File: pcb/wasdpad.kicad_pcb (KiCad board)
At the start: 2 copper layers, 64.2 x 61.2 mm, 24 parts, among them SW1 SW_Push_45deg, SW2 SW_Push_45deg, SW3 SW_Push_45deg, SW4 SW_Push_45deg, SW5 SW_Push_45deg, SW6 SW_Push_45deg, U1 XIAO-RP2040-DIP

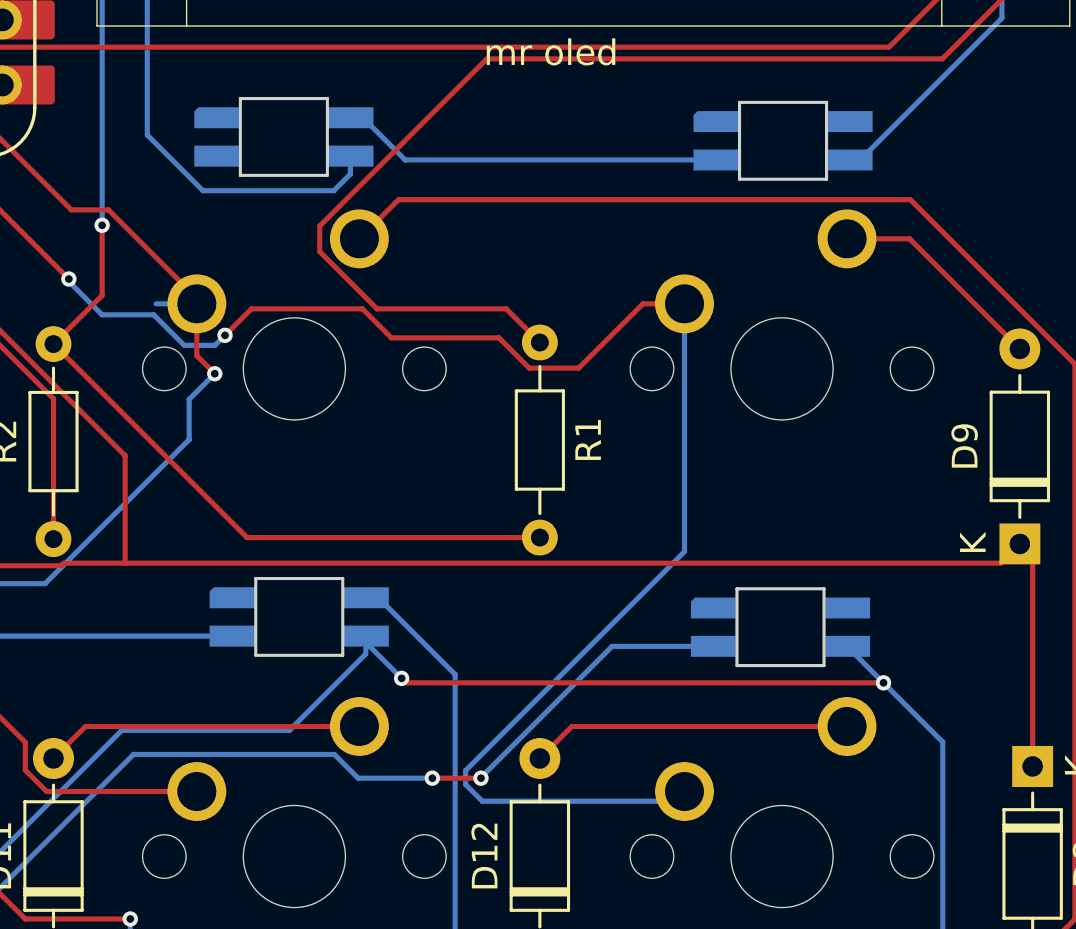
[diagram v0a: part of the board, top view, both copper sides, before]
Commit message: fix unconnected neopixel
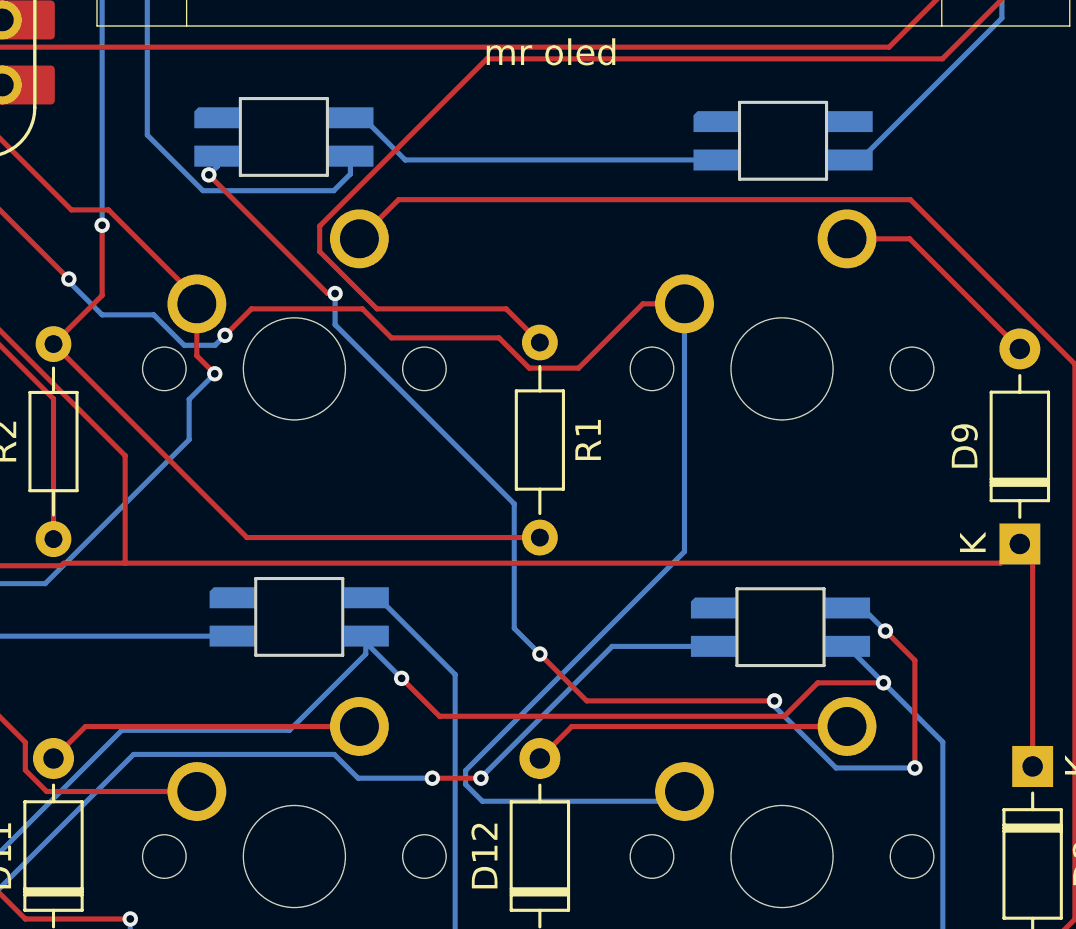
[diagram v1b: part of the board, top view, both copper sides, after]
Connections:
- D13 pad 3: unconnected-(D13-DIN-Pad3) -> Net-(D13-DIN)
- D6 pad 1: unconnected-(D6-DOUT-Pad1) -> Net-(D13-DIN)
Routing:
- net Net-(D13-DIN): track 0.00 -> 49.4 mm, vias 0 -> 6
- net Col 1: track 66.2 -> 64.7 mm
- net +5V: track 295.3 -> 296.4 mm
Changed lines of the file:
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@@
 	(net 28 "unconnected-(U1-GPIO1{slash}RX-Pad8)_1")
 	(net 29 "Net-(D13-DOUT)")
-	(net 30 "unconnected-(D6-DOUT-Pad1)")
-	(net 31 "unconnected-(D13-DIN-Pad3)")
-	(net 32 "unconnected-(D14-DOUT-Pad1)")
+	(net 30 "Net-(D13-DIN)")
+	(net 31 "unconnected-(D14-DOUT-Pad1)")
 	(footprint "oled:SSD1306-0.91-OLED-4pin-128x32"
 		(layer "F.Cu")
@@
 			(size 1.8 0.82)
 			(layers "B.Cu" "B.Paste" "B.Mask")
-			(net 30 "unconnected-(D6-DOUT-Pad1)")
+			(net 30 "Net-(D13-DIN)")
 			(pinfunction "DOUT")
 			(pintype "output")
@@
 			(size 1.8 0.82)
 			(layers "B.Cu" "B.Paste" "B.Mask")
-			(net 31 "unconnected-(D13-DIN-Pad3)")
+			(net 30 "Net-(D13-DIN)")
 			(pinfunction "DIN")
 			(pintype "input")
@@
 			(size 1.8 0.82)
 			(layers "B.Cu" "B.Paste" "B.Mask")
-			(net 32 "unconnected-(D14-DOUT-Pad1)")
+			(net 31 "unconnected-(D14-DOUT-Pad1)")
 			(pinfunction "DOUT")
 			(pintype "output+no_connect")
@@
 	)
 	(segment
+		(start 125.855 117.675)
+		(end 128.425 117.675)
+		(width 0.2)
+		(layer "F.Cu")
+		(net 3)
+	)
+	(segment
 		(start 110.1 131.1)
 		(end 113.05 134.05)
@@
 	)
 	(segment
-		(start 109.775 117.675)
-		(end 128.425 117.675)
+		(start 111.08 118.98)
+		(end 124.55 118.98)
 		(width 0.2)
 		(layer "F.Cu")
@@
 	)
 	(segment
-		(start 109.6 117.5)
-		(end 109.775 117.675)
-		(width 0.2)
-		(layer "F.Cu")
-		(net 3)
-	)
-	(segment
 		(start 94.9 126.9)
 		(end 99 126.9)
@@
 	)
 	(segment
+		(start 109.6 117.5)
+		(end 111.08 118.98)
+		(width 0.2)
+		(layer "F.Cu")
+		(net 3)
+	)
+	(segment
 		(start 99.665 83.66737)
 		(end 95.07763 79.08)
@@
 		(net 3)
 	)
+	(segment
+		(start 124.55 118.98)
+		(end 125.855 117.675)
+		(width 0.2)
+		(layer "F.Cu")
+		(net 3)
+	)
 	(via
 		(at 107.45 129.45)
@@
 	)
 	(segment
-		(start 101.6 102.87)
-		(end 100.01 102.87)
-		(width 0.2)
-		(layer "B.Cu")
-		(net 21)
-	)
-	(segment
 		(start 95.674214 113.8)
 		(end 92.2 113.8)
@@
 		(net 29)
 	)
+	(segment
+		(start 129.65 116.8)
+		(end 128.5 115.65)
+		(width 0.2)
+		(layer "F.Cu")
+		(net 30)
+	)
+	(segment
+		(start 106.70463 102.4661)
+		(end 107 102.4661)
+		(width 0.2)
+		(layer "F.Cu")
+		(net 30)
+	)
+	(segment
+		(start 129.65 121)
+		(end 129.65 116.8)
+		(width 0.2)
+		(layer "F.Cu")
+		(net 30)
+	)
+	(segment
+		(start 116.83 118.38)
+		(end 124.165735 118.38)
+		(width 0.2)
+		(layer "F.Cu")
+		(net 30)
+	)
+	(segment
+		(start 102.069265 97.830735)
+		(end 106.70463 102.4661)
+		(width 0.2)
+		(layer "F.Cu")
+		(net 30)
+	)
+	(segment
+		(start 115 116.55)
+		(end 116.83 118.38)
+		(width 0.2)
+		(layer "F.Cu")
+		(net 30)
+	)
+	(via
+		(at 124.165735 118.38)
+		(size 0.6)
+		(drill 0.3)
+		(layers "F.Cu" "B.Cu")
+		(net 30)
+	)
+	(via
+		(at 129.65 121)
+		(size 0.6)
+		(drill 0.3)
+		(layers "F.Cu" "B.Cu")
+		(net 30)
+	)
+	(via
+		(at 107 102.4661)
+		(size 0.6)
+		(drill 0.3)
+		(layers "F.Cu" "B.Cu")
+		(net 30)
+	)
+	(via
+		(at 128.5 115.65)
+		(size 0.6)
+		(drill 0.3)
+		(layers "F.Cu" "B.Cu")
+		(net 30)
+	)
+	(via
+		(at 115 116.55)
+		(size 0.6)
+		(drill 0.3)
+		(layers "F.Cu" "B.Cu")
+		(net 30)
+	)
+	(via
+		(at 102.069265 97.830735)
+		(size 0.6)
+		(drill 0.3)
+		(layers "F.Cu" "B.Cu")
+		(net 30)
+	)
+	(segment
+		(start 102.4 97.1)
+		(end 102.4 97.5)
+		(width 0.2)
+		(layer "B.Cu")
+		(net 30)
+	)
+	(segment
+		(start 124.165735 118.596345)
+		(end 126.56939 121)
+		(width 0.2)
+		(layer "B.Cu")
+		(net 30)
+	)
+	(segment
+		(start 128.5 115.65)
+		(end 127.6 114.75)
+		(width 0.2)
+		(layer "B.Cu")
+		(net 30)
+	)
+	(segment
+		(start 124.165735 118.38)
+		(end 124.165735 118.596345)
+		(width 0.2)
+		(layer "B.Cu")
+		(net 30)
+	)
+	(segment
+		(start 107 102.4661)
+		(end 107 103.685225)
+		(width 0.2)
+		(layer "B.Cu")
+		(net 30)
+	)
+	(segment
+		(start 107 103.685225)
+		(end 114 110.685225)
+		(width 0.2)
+		(layer "B.Cu")
+		(net 30)
+	)
+	(segment
+		(start 127.6 114.75)
+		(end 127 114.75)
+		(width 0.2)
+		(layer "B.Cu")
+		(net 30)
+	)
+	(segment
+		(start 102.4 97.5)
+		(end 102.069265 97.830735)
+		(width 0.2)
+		(layer "B.Cu")
+		(net 30)
+	)
+	(segment
+		(start 114 110.685225)
+		(end 114 115.55)
+		(width 0.2)
+		(layer "B.Cu")
+		(net 30)
+	)
+	(segment
+		(start 126.56939 121)
+		(end 129.65 121)
+		(width 0.2)
+		(layer "B.Cu")
+		(net 30)
+	)
+	(segment
+		(start 114 115.55)
+		(end 115 116.55)
+		(width 0.2)
+		(layer "B.Cu")
+		(net 30)
+	)
 	(zone

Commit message: add production files
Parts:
- added G***: LOGO, LOGO, F.Cu at (116.6, 85.9)
- added G***: LOGO, LOGO, B.Cu at (125.6, 86.0)
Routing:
- net Col 1: track 64.7 -> 63.5 mm
- net Col 2: vias 4 -> 5
- net Net-(D1-DOUT): vias 0 -> 2
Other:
- board text added: "a macropad with 6 inputs, rgb and an oled!"
- board text added: "obob's wasdpad"
- board text added: "yummy cherries"

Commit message: fix silkscreen
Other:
- board text added: "github.com/DaBlower/wasdpad"
- board text added: "star and follow me on github!"
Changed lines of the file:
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@@
 		)
 		(fp_text user "OLED Panel"
-			(at 19 6 0)
+			(at 23.39 1.675 0)
 			(layer "F.SilkS")
 			(effects
@@
 		)
 	)
+	(gr_text "star and follow\nme on github!"
+		(at 110.88 91.78 -0)
+		(layer "B.SilkS")
+		(effects
+			(font
+				(size 0.8 0.8)
+				(thickness 0.2)
+				(bold yes)
+			)
+			(justify left bottom mirror)
+		)
+	)
 	(gr_text "a macropad with 6 inputs,\nrgb and an oled!"
 		(at 118.35 87.02 -0)
@@
 		)
 	)
+	(gr_text "star and follow\nme on github!"
+		(at 101.28 91.8 0)
+		(layer "F.SilkS")
+		(effects
+			(font
+				(size 0.8 0.8)
+				(thickness 0.2)
+				(bold yes)
+			)
+			(justify left bottom)
+		)
+	)
 	(gr_text "yummy cherries"
 		(at 115.52 110.72 0)
@@
 			)
 			(justify left bottom)
+		)
+	)
+	(gr_text "github.com/DaBlower/wasdpad"
+		(at 111.55 91.65 0)
+		(layer "F.SilkS")
+		(effects
+			(font
+				(size 0.8 0.8)
+				(thickness 0.1)
+			)
+			(justify left bottom)
